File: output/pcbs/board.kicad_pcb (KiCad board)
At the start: 2 copper layers, 169.9 x 163.3 mm, 89 parts

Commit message: Added board text to silkscreen
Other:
- board text added: "Ergo-Nano"
- board text added: "Left Hand"
- board text added: "Right Hand"
- board text added: "V1.0"
- board text added: "by Aevum Decessus"
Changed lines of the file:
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@@
     (pad "1" thru_hole circle (at 3.25 0 90) (size 1.7 1.7) (drill 1.0) (layers "*.Cu" "*.Mask") (net 56 "RST"))
+  )
+  (gr_text "Ergo-Nano"
+    (at 59.525 37.57 0)
+    (layer "F.SilkS" )
+    (effects
+      (font
+        (size 3 3)
+        (thickness 0.15)
+        (bold yes)
+      )
+    )
+  )
+  (gr_text "Ergo-Nano"
+    (at 59.525 37.57 0)
+    (layer "B.SilkS" )
+    (effects
+      (font
+        (size 3 3)
+        (thickness 0.15)
+        (bold yes)
+      )
+      (justify  mirror)
+    )
+  )
+  (gr_text "V1.0"
+    (at 88 34.475 0)
+    (layer "F.SilkS" )
+    (effects
+      (font
+        (size 3 3)
+        (thickness 0.15)
+        (bold yes)
+      )
+    )
+  )
+  (gr_text "V1.0"
+    (at 88 34.475 0)
+    (layer "B.SilkS" )
+    (effects
+      (font
+        (size 3 3)
+        (thickness 0.15)
+        (bold yes)
+      )
+      (justify  mirror)
+    )
+  )
+  (gr_text "by Aevum Decessus"
+    (at 61.43 41.38 0)
+    (layer "F.SilkS" )
+    (effects
+      (font
+        (size 1 1)
+        (thickness 0.15)
+      )
+    )
+  )
+  (gr_text "by Aevum Decessus"
+    (at 61.43 41.38 0)
+    (layer "B.SilkS" )
+    (effects
+      (font
+        (size 1 1)
+        (thickness 0.15)
+      )
+      (justify  mirror)
+    )
+  )
+  (gr_text "Left Hand"
+    (at 149.7625 39.475 0)
+    (layer "F.SilkS" )
+    (effects
+      (font
+        (size 3 3)
+        (thickness 0.15)
+        (bold yes)
+      )
+    )
+  )
+  (gr_text "Right Hand"
+    (at 149.7625 39.475 0)
+    (layer "B.SilkS" )
+    (effects
+      (font
+        (size 3 3)
+        (thickness 0.15)
+        (bold yes)
+      )
+      (justify  mirror)
+    )
   )
   (footprint "ceoloide:mounting_hole_npth"

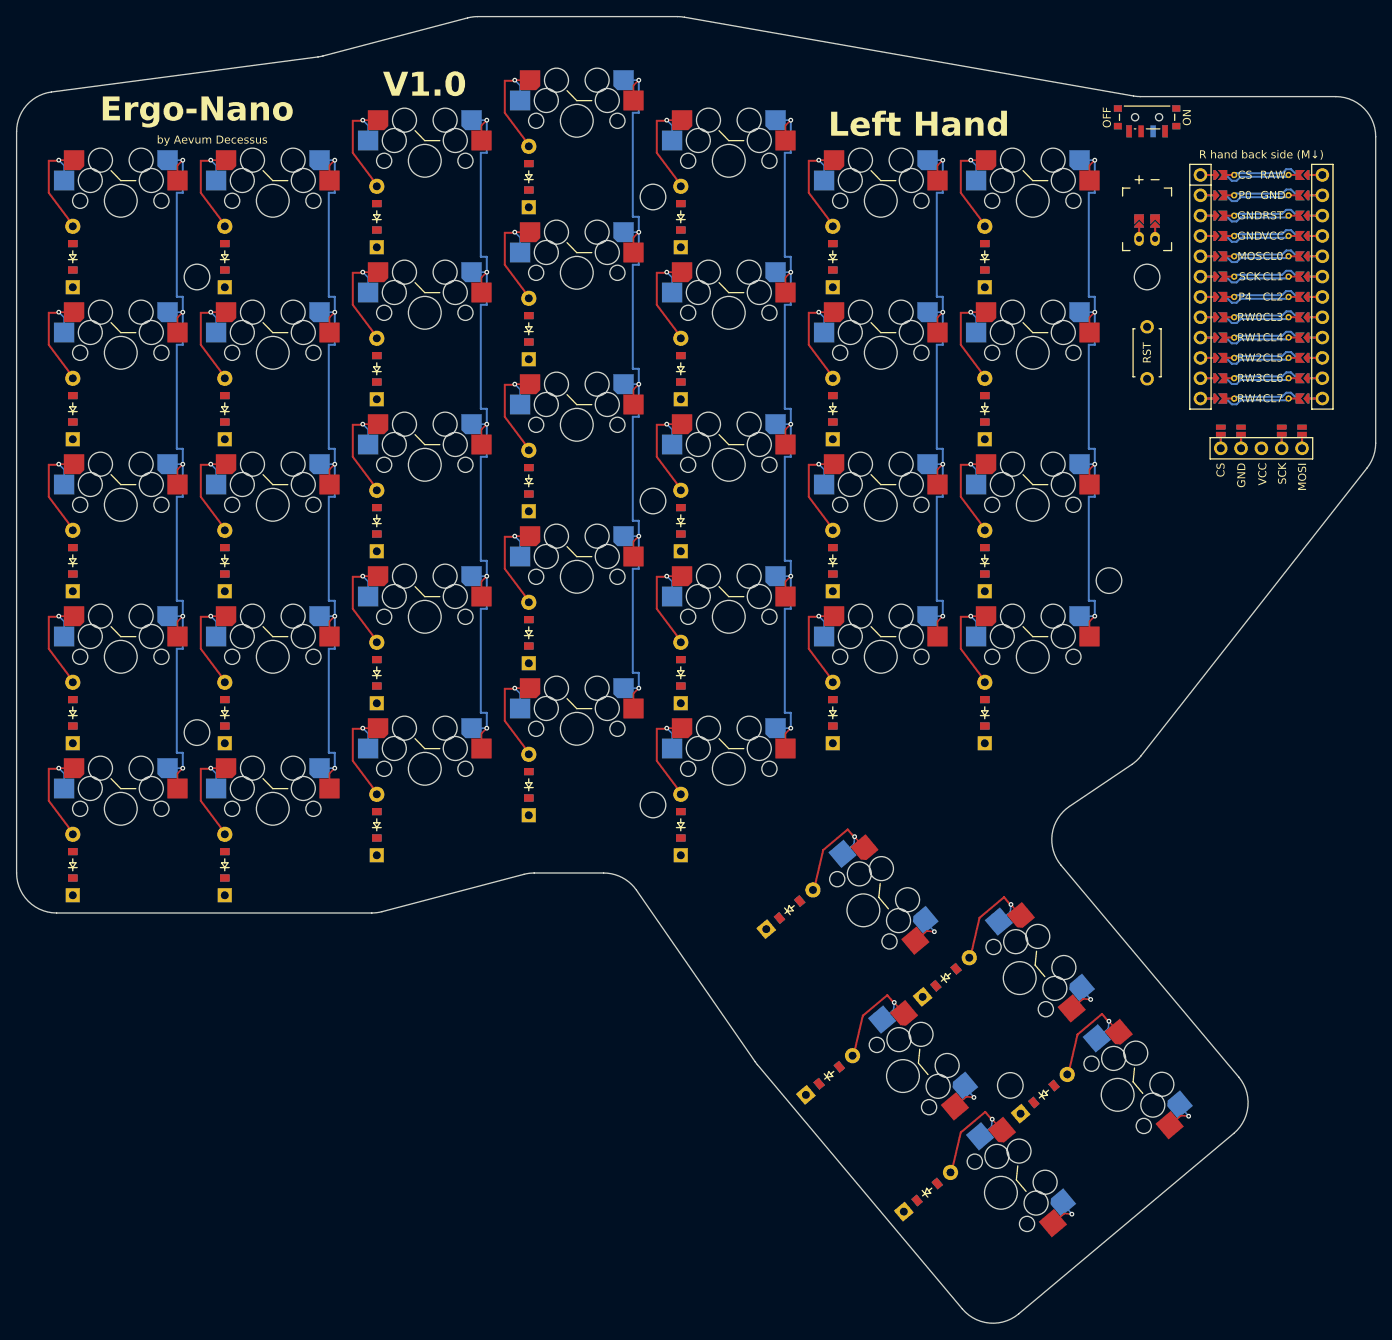
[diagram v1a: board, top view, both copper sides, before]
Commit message: Removed the 90 degree traces for columns and diodes
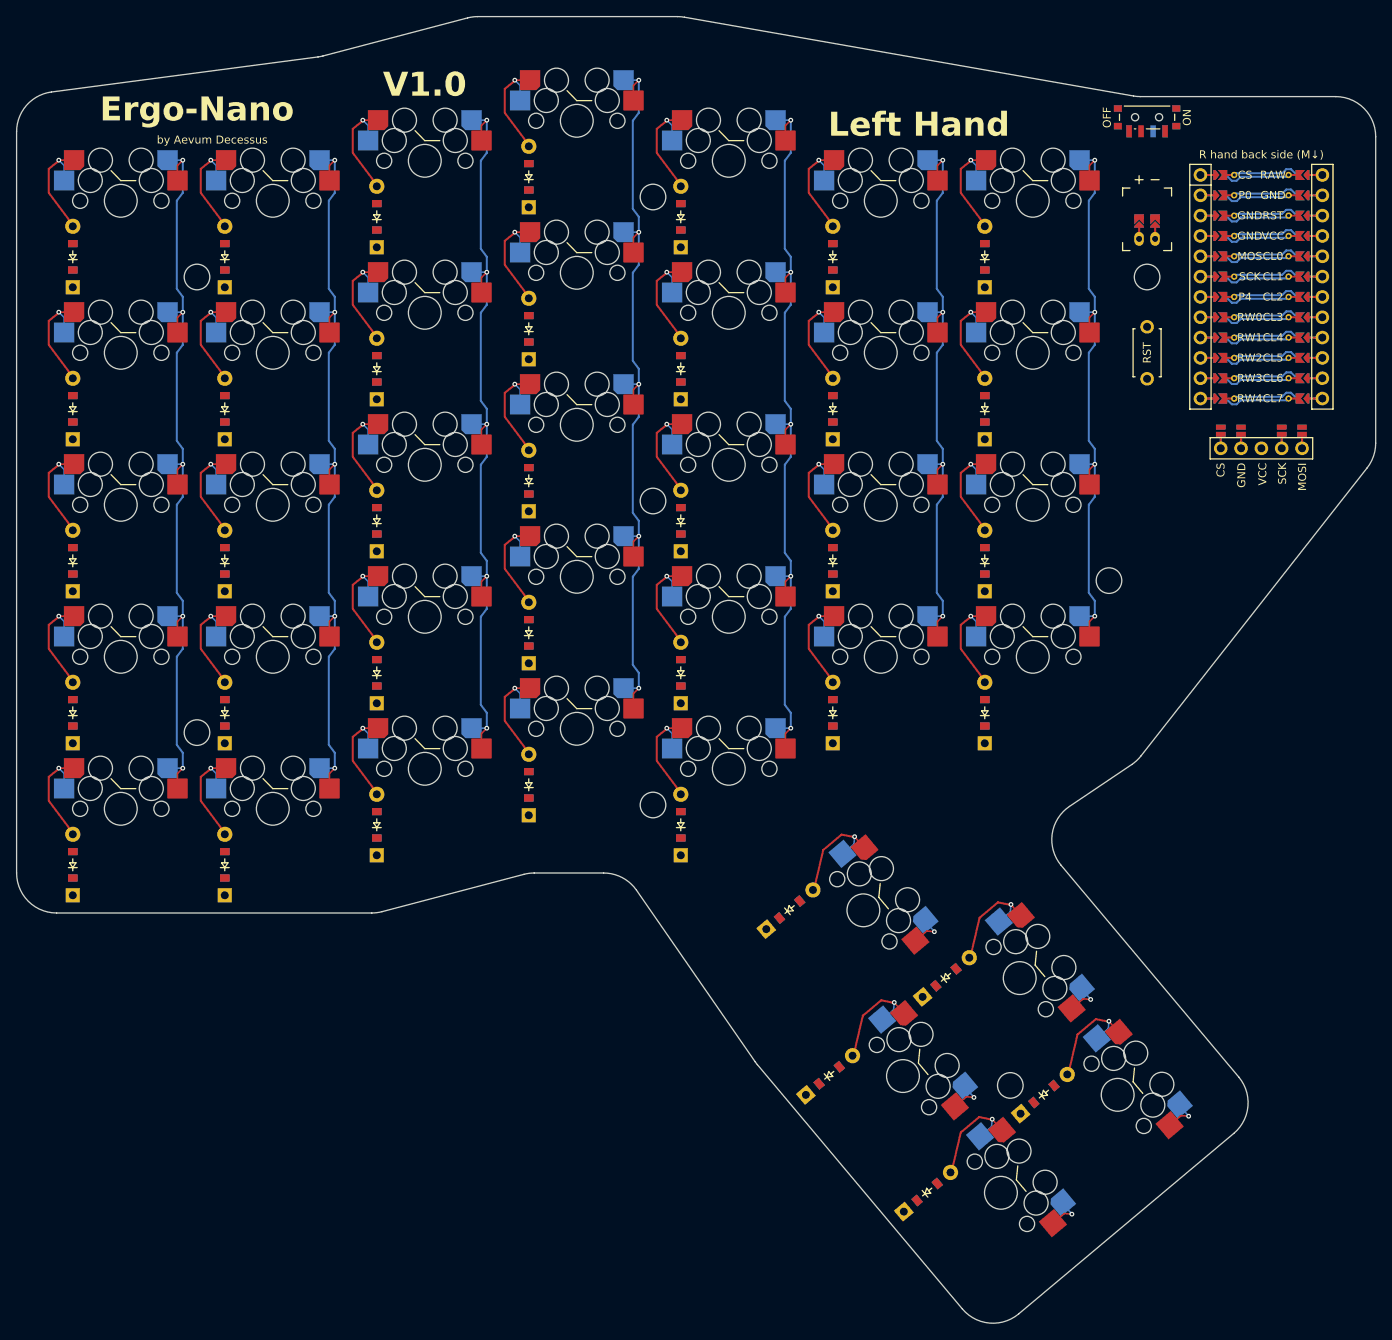
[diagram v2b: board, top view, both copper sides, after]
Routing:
- net (no net): track 878.4 -> 852.4 mm
- net ring_top: track 15.0 -> 14.3 mm
- net ring_num: track 15.0 -> 14.3 mm
- net ring_mod: track 15.0 -> 14.3 mm
- net ring_home: track 15.0 -> 14.3 mm
- net ring_bottom: track 15.0 -> 14.3 mm
- net pinky_top: track 15.0 -> 14.3 mm
- net pinky_num: track 15.0 -> 14.3 mm
- net pinky_mod: track 15.0 -> 14.3 mm
- net pinky_home: track 15.0 -> 14.3 mm
- net pinky_bottom: track 15.0 -> 14.3 mm
- net outer_top: track 15.0 -> 14.3 mm
- net outer_num: track 15.0 -> 14.3 mm
- net outer_mod: track 15.0 -> 14.3 mm
- net outer_home: track 15.0 -> 14.3 mm
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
